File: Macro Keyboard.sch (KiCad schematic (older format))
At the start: 0 parts

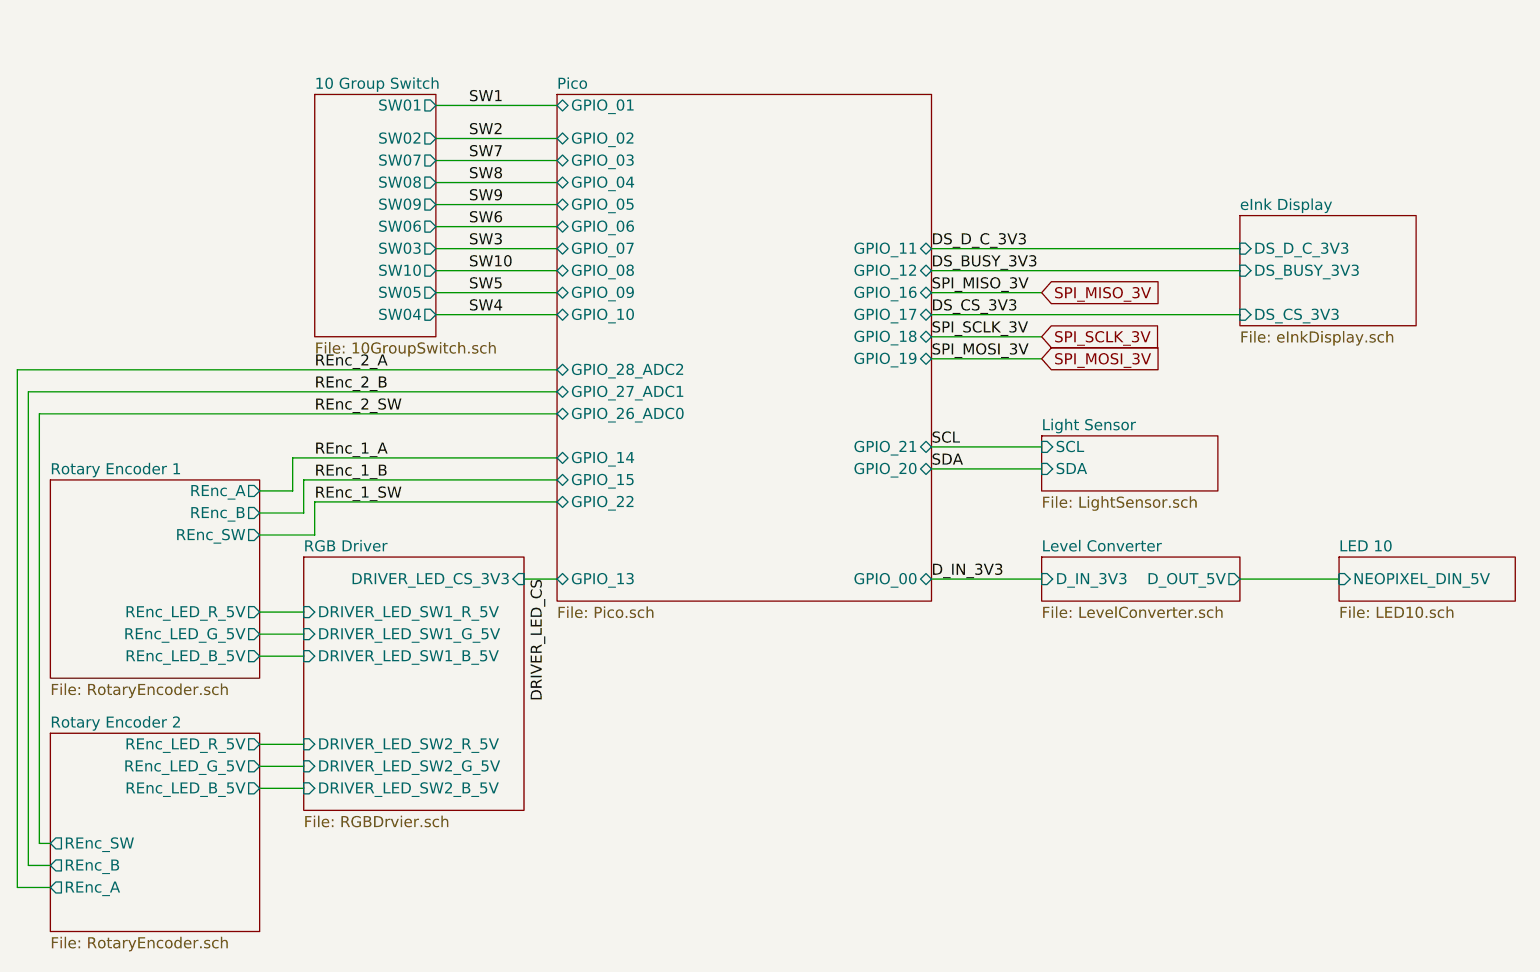
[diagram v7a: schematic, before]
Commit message: Updated so that eink reset pin is shared with GP04. Not ideal, but should work.
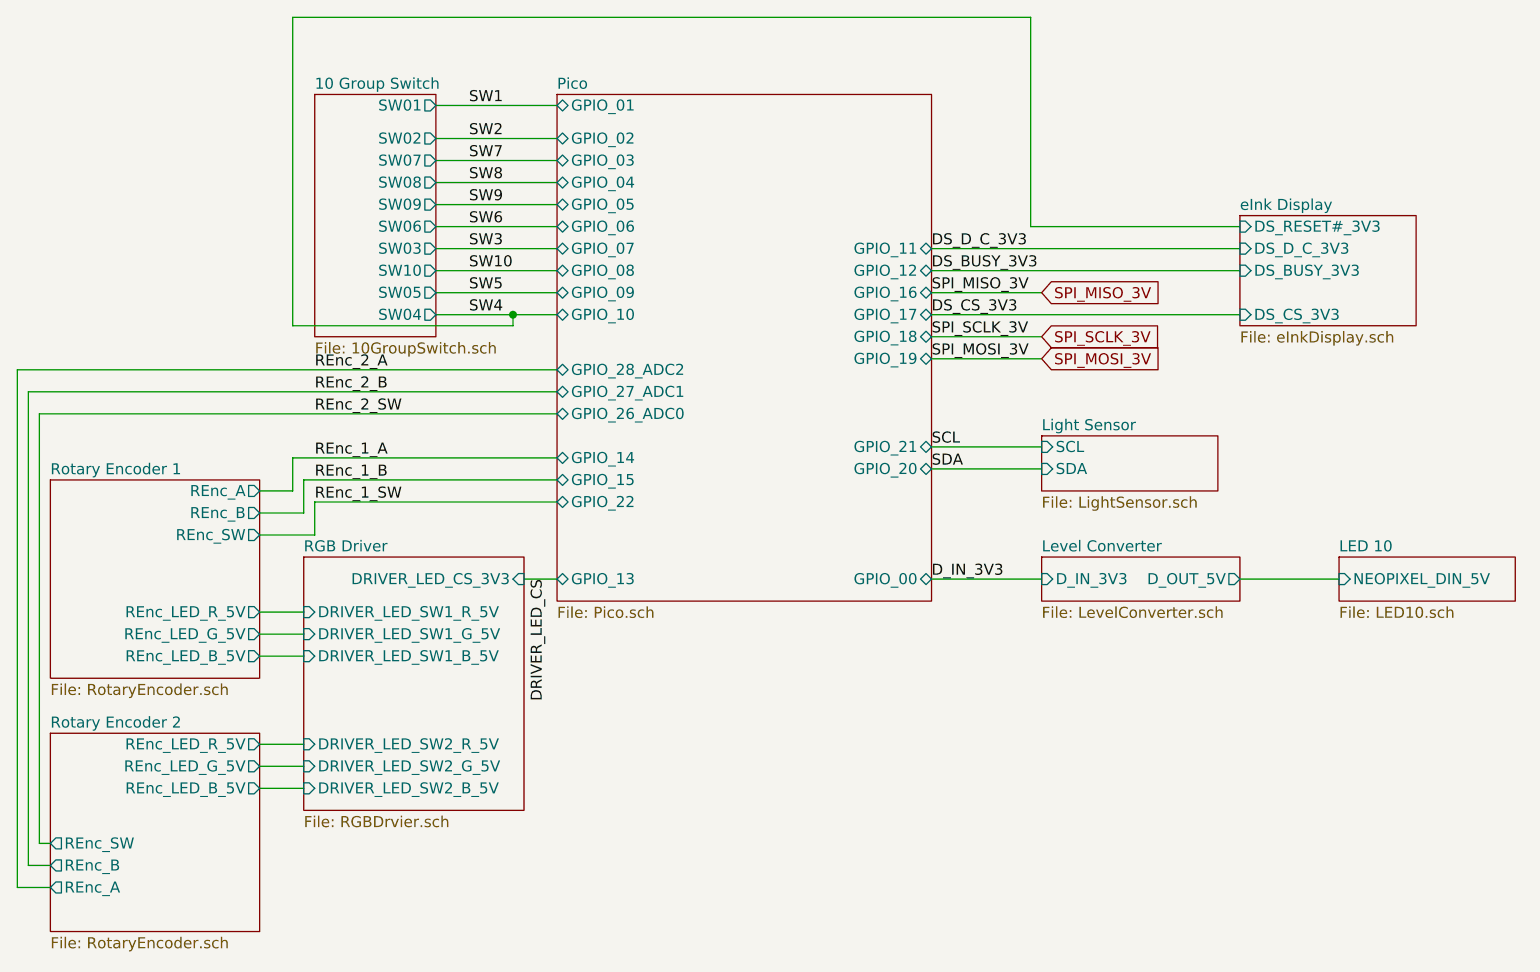
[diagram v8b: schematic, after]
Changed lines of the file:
@@
 	3550 3050 3000 3050
 Wire Wire Line
-	3000 3150 3550 3150
+	3000 3150 3350 3150
 $Sheet
 S 6650 2700 800  500
@@
 F3 "DS_D_C_3V3" I L 6650 2850 50
 F4 "DS_BUSY_3V3" I L 6650 2950 50
+F5 "DS_RESET#_3V3" I L 6650 2750 50
 $EndSheet
 Wire Wire Line
@@
 F27 "GPIO_28_ADC2" B L 3550 3400 50
 $EndSheet
+Wire Wire Line
+	6650 2750 5700 2750
+Wire Wire Line
+	5700 2750 5700 1800
+Wire Wire Line
+	5700 1800 2350 1800
+Wire Wire Line
+	2350 1800 2350 3200
+Wire Wire Line
+	2350 3200 3350 3200
+Wire Wire Line
+	3350 3200 3350 3150
+Connection ~ 3350 3150
+Wire Wire Line
+	3350 3150 3550 3150
 $EndSCHEMATC
